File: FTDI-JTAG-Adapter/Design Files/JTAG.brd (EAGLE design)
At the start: 50 x 29 mm, 10 parts

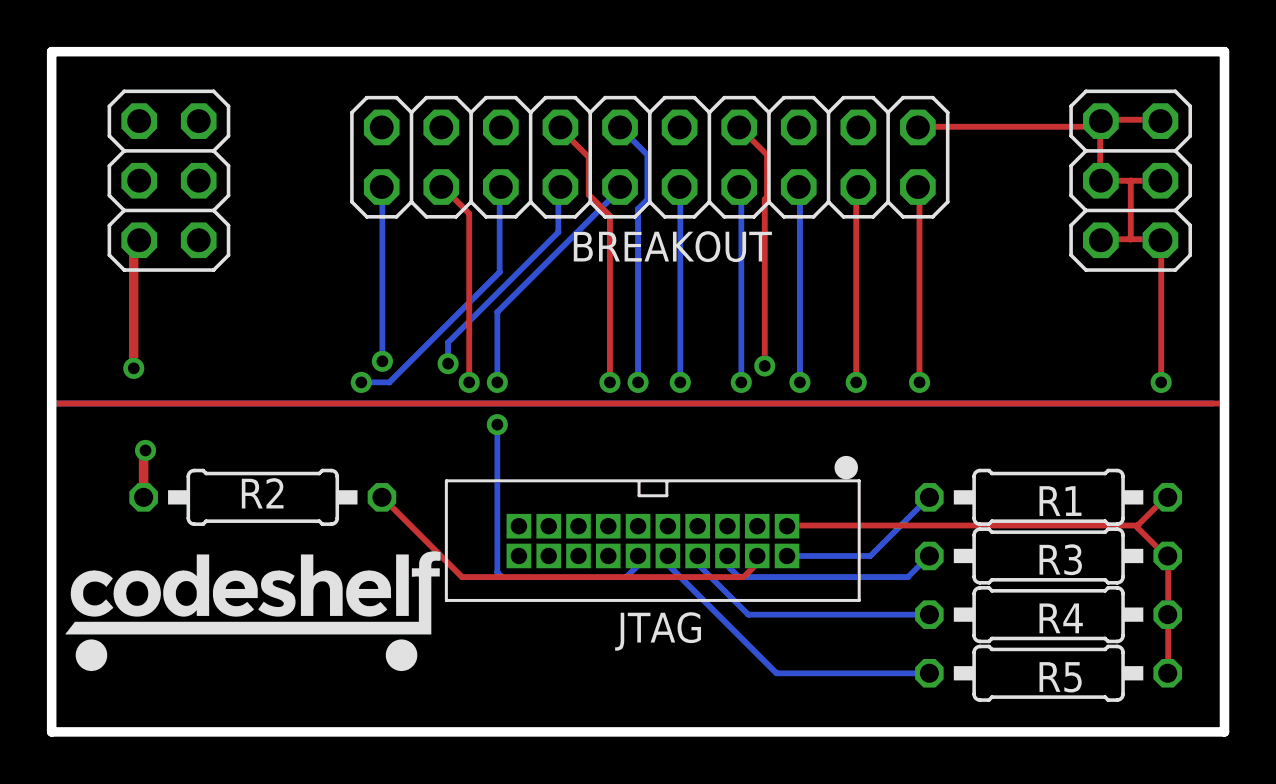
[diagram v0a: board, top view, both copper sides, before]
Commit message: Change the FTDI-JTAG vias to 0.25mm
Chris asked for this.
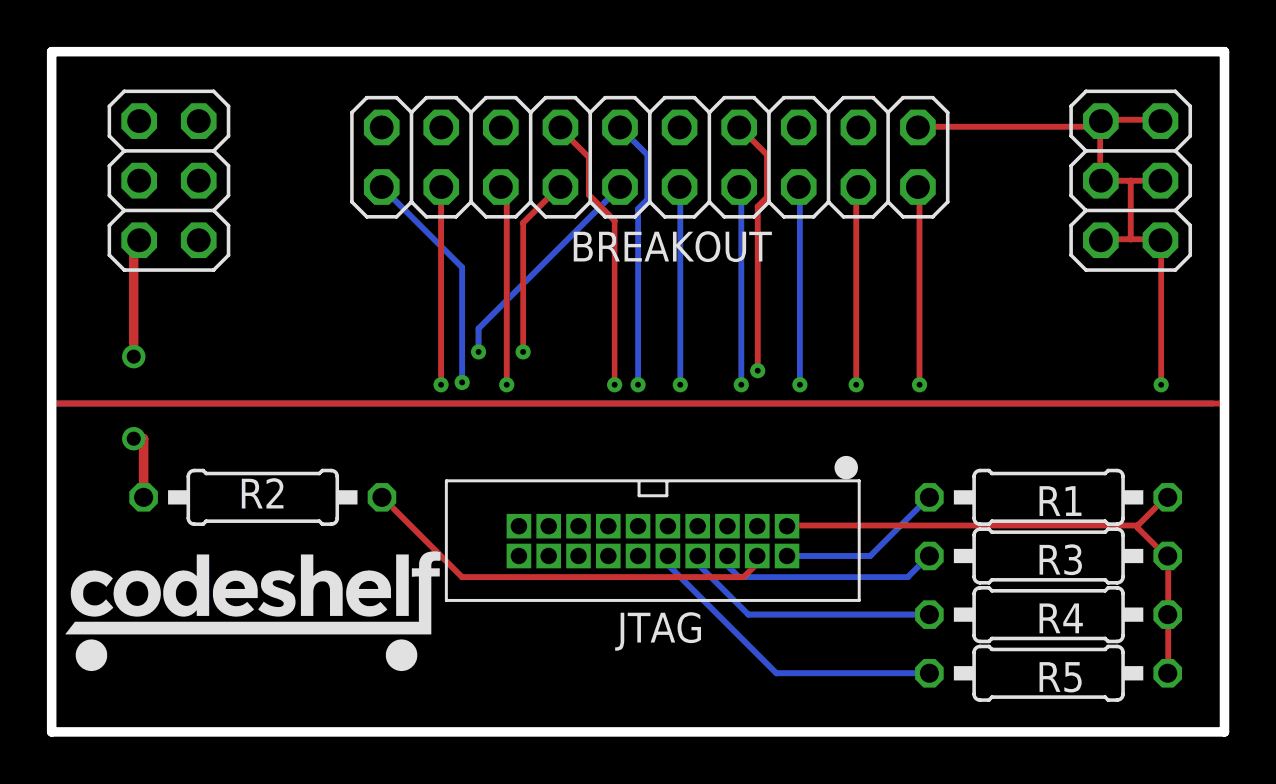
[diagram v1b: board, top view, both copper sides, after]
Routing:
- net N$9: track 25.8 -> 20.5 mm
- net N$7: track 25.4 -> 29.1 mm, vias 2 -> 1
- net N$8: track 25.3 -> 24.1 mm
